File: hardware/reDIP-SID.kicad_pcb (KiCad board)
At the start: 4 copper layers, 17.8 x 35.6 mm, 90 parts, among them J1 Conn_01x04, J2 Conn_01x04, J3 Conn_01x10, J4 Conn_01x10, J5 TYPE-C-31-M-12, J6 Conn_02x05_Odd_Even, SW1 KXT331LHS, U1 NCP115AMX120TCG, U2 NCP167AMX330TBG, U3 SN74CBTD16211DGVR, U4 SGTL5000XNLA3, U5 NUF2042XV6, U6 APS6404L-3SQR-SN, U7 W25Q128JVPIM, U8 ICE40UP5K-SG48I, X1 ECS-1612MV-240-CN-TR

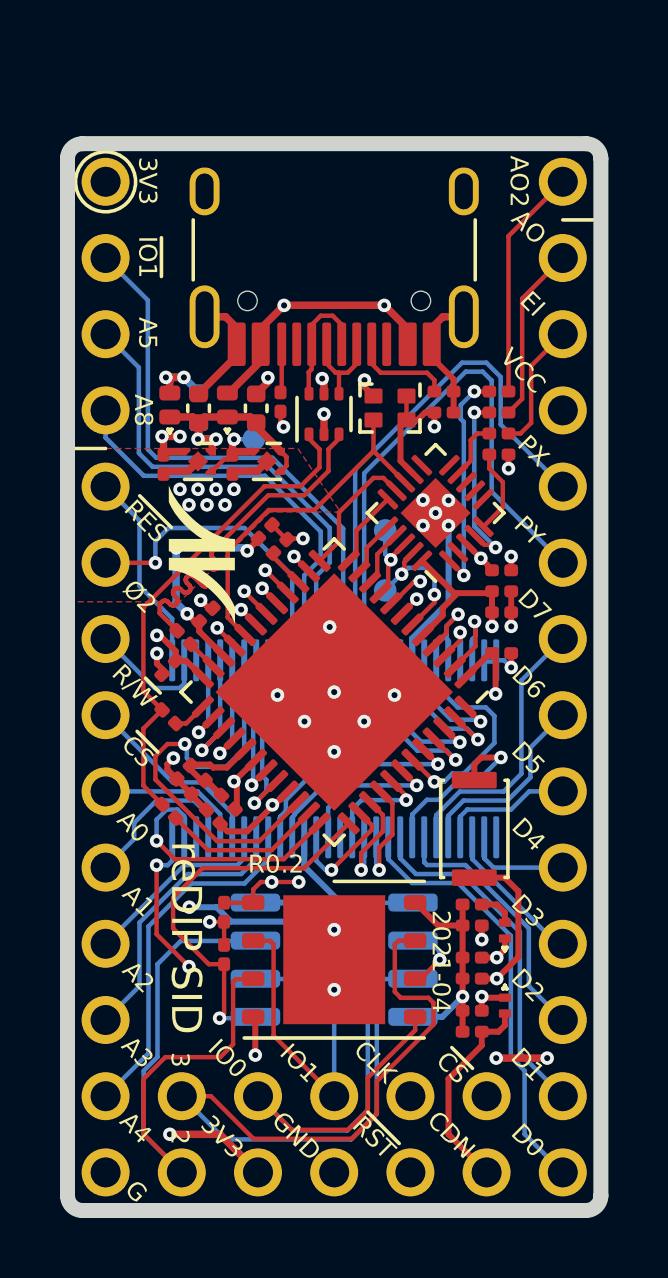
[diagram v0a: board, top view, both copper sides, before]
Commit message: Revision 1.0
The board has been revised to remedy a few shortcomings on the first prototype:

* Added a separate LDO for the SGTL5000 VDDD, to keep the iCE40 VCC at 1.2V.
* Added DC bias for AUDIO_OUT, required by the C64 audio output stage.
* Increased board length by 2.54mm, facilitating some notable enhancements:
  - Symmetric stereo input (EXT_IN and EXT_IN_R). Note: External AC coupling.
  - Symmetric stereo output (AOUT_L and AOUT_R) in addition to AUDIO_OUT.
  - USB receptacle flush with board edge.
  - Fully 6581 / 8580 pin compatible.

Big thanks go to @smunaut, who has not only implemented support for the
reDIP SID in his [no2bootloader](https://github.com/no2fpga/no2bootloader),
but has also provided invaluable feedback from his testing of prototypes.
He pointed out that the internal SGTL5000 voltage regulator forced the
1.2V rail up to unsafe levels for the iCE40, and that DC bias is required
to drive the C64 audio output stage. He also suggested to add symmetric
stereo output, in addition to the SID audio output.
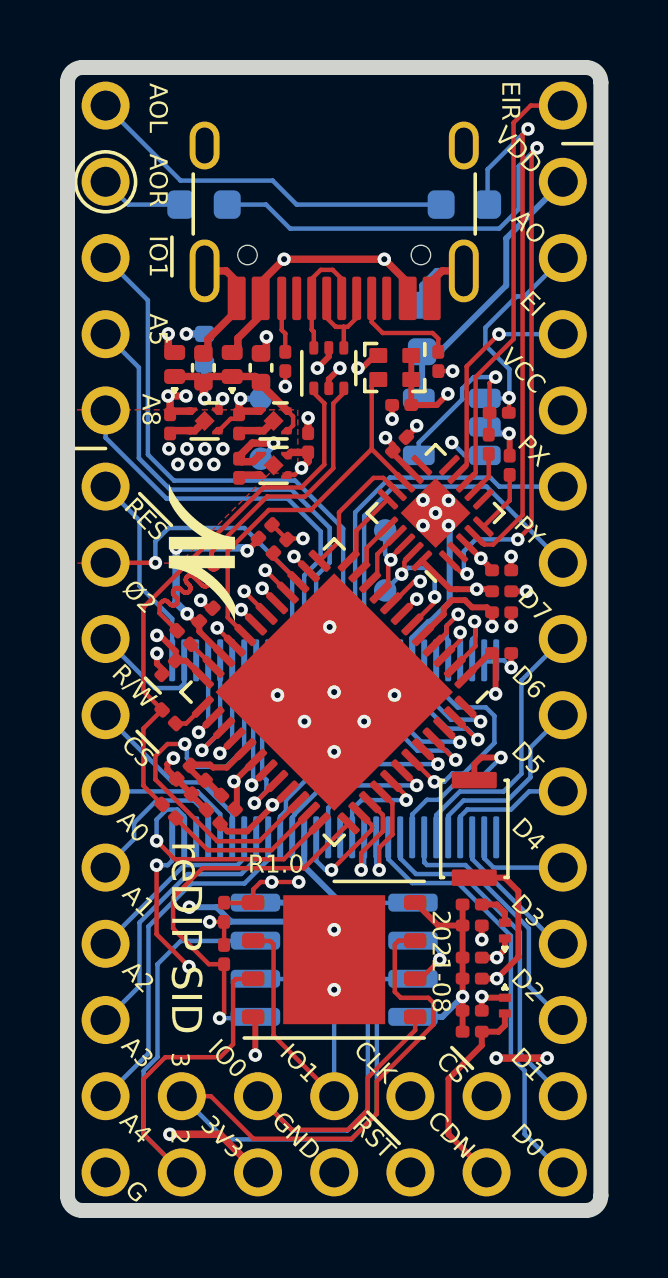
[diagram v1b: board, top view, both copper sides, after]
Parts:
- removed the C10 at (113.1, 107.7)
- removed the C15 at (113.2, 114.3)
- removed the C8 at (113.1, 108.4)
- removed the C9 at (113.1, 107.0)
- removed the J4 at (115.2, 110.2)
- removed the R4 at (105.8, 107.3)
- removed the SolderMask D0.5mm at (103.4, 110.8) (x2)
- removed the SolderMask D0.5mm at (102.8, 110.8) (x2)
- removed the SolderMask D0.5mm at (102.5, 110.2)
- removed the SolderMask D0.5mm at (103.1, 110.2) (x2)
- removed the SolderMask D0.5mm at (103.7, 110.2) (x2)
- removed the SolderMask D0.5mm at (104.0, 110.8) (x2)
- removed the SolderMask D0.5mm at (105.7, 117.1)
- removed the SolderMask D0.5mm at (107.6, 119.0)
- removed the SolderMask D0.5mm at (108.6, 118.0)
- removed the SolderMask D0.5mm at (109.6, 117.1)
- removed the SolderMask D0.5mm at (107.5, 114.8)
- removed the SolderMask D0.5mm at (107.6, 117.0)
- removed the SolderMask D0.5mm at (106.6, 118.0)
- removed the SolderMask D0.5mm at (104.3, 110.2)
- added C11: 1uF, Capacitor_SMD:C_0603_1608Metric, B.Cu at (110.5, 104.9)
- added C12: 10uF, Capacitor_SMD:C_0603_1608Metric, B.Cu at (103.3, 100.8)
- added C13: 10uF, Capacitor_SMD:C_0603_1608Metric, B.Cu at (112.0, 100.8)
- added C23: 0.1uF, Capacitor_SMD:C_0201_0603Metric, F.Cu at (109.9, 107.4)
- added C5: 1uF, Capacitor_SMD:C_0201_0603Metric, F.Cu at (106.8, 108.7)
- added C6: 1uF, Capacitor_SMD:C_0201_0603Metric, F.Cu at (104.5, 109.5)
- added C7: 0.1uF, Capacitor_SMD:C_0201_0603Metric, F.Cu at (113.2, 113.7)
- added J3: Conn_01x14, reDIP:PinHeader_1x14_P2.54mm_Vertical, B.Cu at (115.2, 100.0)
- added R3: 10k, Resistor_SMD:R_0201_0603Metric, F.Cu at (112.8, 108.8)
- added R5: 10k, Resistor_SMD:R_0201_0603Metric, F.Cu at (113.1, 107.7)
- added R6: 5.1k, Resistor_SMD:R_0201_0603Metric, F.Cu at (106.0, 106.0)
- added SolderMask D0.5mm: SolderMask_D0.5mm, reDIP:SolderMask_D0.5mm, B.Cu at (103.0, 109.4)
- added SolderMask D0.5mm: SolderMask_D0.5mm, reDIP:SolderMask_D0.5mm, B.Cu at (102.4, 109.4)
- added SolderMask D0.5mm: SolderMask_D0.5mm, reDIP:SolderMask_D0.5mm, B.Cu at (102.1, 108.9)
- added SolderMask D0.5mm: SolderMask_D0.5mm, reDIP:SolderMask_D0.5mm, B.Cu at (102.7, 108.9)
- added SolderMask D0.5mm: SolderMask_D0.5mm, reDIP:SolderMask_D0.5mm, B.Cu at (103.3, 108.9)
- added SolderMask D0.5mm: SolderMask_D0.5mm, reDIP:SolderMask_D0.5mm, B.Cu at (103.6, 109.4)
- added SolderMask D0.5mm: SolderMask_D0.3mm, reDIP:SolderMask_D0.3mm, F.Cu at (103.6, 109.4)
- added SolderMask D0.5mm: SolderMask_D0.3mm, reDIP:SolderMask_D0.3mm, F.Cu at (103.0, 109.4)
- added SolderMask D0.5mm: SolderMask_D0.3mm, reDIP:SolderMask_D0.3mm, F.Cu at (102.4, 109.4)
- added SolderMask D0.5mm: SolderMask_D0.3mm, reDIP:SolderMask_D0.3mm, F.Cu at (103.9, 108.9)
- added SolderMask D0.5mm: SolderMask_D0.3mm, reDIP:SolderMask_D0.3mm, F.Cu at (103.3, 108.9)
- added SolderMask D0.5mm: SolderMask_D0.3mm, reDIP:SolderMask_D0.3mm, F.Cu at (102.7, 108.9)
- added SolderMask_D0.3mm: SolderMask_D0.3mm, reDIP:SolderMask_D0.3mm, B.Cu at (107.6, 119.0)
- added SolderMask_D0.3mm: SolderMask_D0.3mm, reDIP:SolderMask_D0.3mm, B.Cu at (108.6, 118.0)
- added SolderMask_D0.3mm: SolderMask_D0.3mm, reDIP:SolderMask_D0.3mm, B.Cu at (106.6, 118.0)
- added SolderMask_D0.3mm: SolderMask_D0.3mm, reDIP:SolderMask_D0.3mm, B.Cu at (109.6, 117.1)
- added SolderMask_D0.3mm: SolderMask_D0.3mm, reDIP:SolderMask_D0.3mm, B.Cu at (107.6, 117.0)
- added SolderMask_D0.3mm: SolderMask_D0.3mm, reDIP:SolderMask_D0.3mm, B.Cu at (105.7, 117.1)
- added SolderMask_D0.3mm: SolderMask_D0.3mm, reDIP:SolderMask_D0.3mm, B.Cu at (107.5, 114.8)
- added TP2: TestPoint_Flag, reDIP:TestPoint_Pad_D0.75mm, B.Cu at (105.2, 109.2)
- added U3: NCP115AMX120TCG, ONSemi:CASE_711AJ_1.0x1.0mm_P0.65mm, F.Cu at (105.6, 109.5)
- added U7: MCP6H01T-E/OT, reDIP:SOT-23-5, B.Cu at (111.5, 108.2)
- added svg2mod: G***, reDIP:Nimrod-N, B.Cu at (108.4, 108.5)
- J1: value Conn_01x04 -> Conn_01x01; footprint reDIP:PinHeader_1x04_P2.54mm_Vertical_LongTail -> reDIP:PinHeader_1x01_P2.54mm_Vertical; moved to F.Cu
- J2: value Conn_01x04 -> Conn_01x05; footprint reDIP:PinHeader_1x04_P2.54mm_Vertical_LongTail -> reDIP:PinHeader_1x05_P2.54mm_Vertical; moved to F.Cu
- U8: renamed from U6; value APS6404L-3SQR-SN -> LY68L6400SLIT
- X1: value ECS-1612MV-240-CN-TR -> ASCO-24.000MHZ-EK-T3
- svg2mod: footprint reDIP:Nimrod-logo -> reDIP:Nimrod-text
- moved J1 15.5 mm to (115.2, 97.5), turned to 0 degrees
- moved J2 15.5 mm to (100.0, 97.5), turned to 0 degrees
- moved svg2mod 2.78 mm to (112.3, 112.5)
- moved JP1 1.96 mm to (103.3, 105.6)
- moved C8 1.81 mm to (109.8, 108.7), turned to 45 degrees
- moved MOS logo 1.55 mm to (106.0, 103.3)
- moved U6 1.54 mm to (107.4, 106.2)
- moved J5 1.53 mm to (107.6, 99.8)
- moved SolderMask D0.5mm 1.40 mm to (103.9, 108.9)
- moved SolderMask D0.5mm 1.40 mm to (102.1, 108.9)
- moved TP1 1.37 mm to (105.2, 107.2)
- moved C2 1.37 mm to (104.5, 108.1)
- moved C4 1.37 mm to (102.2, 108.1)
- moved U1 1.37 mm to (105.6, 108.0)
- moved U2 1.37 mm to (103.3, 108.0)
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- renumbered C7 to C10, C11 to C14, C12 to C15, C13 to C16, C14 to C17, C16 to C18, C17 to C19, C18 to C20, C19 to C21, C20 to C22, C5 to C8, C6 to C9, J3 to J4, R8 to R10, R9 to R11, R10 to R12, R11 to R13, R12 to R14, R13 to R15, R14 to R16, R3 to R4, R5 to R7, R6 to R8, R7 to R9, TP2 to TP3, TP3 to TP4, U8 to U10, U3 to U4, U4 to U5, U5 to U6, U7 to U9
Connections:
- J1 pad 1: +3V3 -> /EXT_IN_R
- J2 pad 1: /AUDIO_OUT_2 -> /AOUT_L
- J2 pad 2: /AUDIO_OUT -> /AOUT_R
- J2 pad 3: /EXT_IN -> /~IO1~
- J2 pad 4: VCC -> /A5
- U5 pad 20: +1V2 -> VDDD
- U5 pad 7: (no net) -> Net-(R3-Pad2)
- U5 pad 8: (no net) -> /EXT_IN_R
- U5 pad 9: Net-(C8-Pad1) -> /EXT_IN
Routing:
- net Net-(C12-Pad1): track 7.55 -> 29.5 mm, vias 2 -> 3
- net VDDD: track 0.00 -> 15.0 mm, vias 0 -> 2
- net /EXT_IN_R: track 0.00 -> 14.5 mm
- net /AOUT_L: track 0.00 -> 12.6 mm
- net Net-(C13-Pad1): track 6.15 -> 18.1 mm, vias 2 -> 1
- net VDD: track 0.00 -> 9.52 mm
- net /AUDIO_OUT_2: track 7.75 -> 0.00 mm
- net /POT_Y: track 19.1 -> 12.9 mm
- net Net-(R3-Pad1): track 0.00 -> 6.11 mm, vias 0 -> 1
- net /POT_X: track 17.4 -> 12.5 mm
- net GND: track 44.9 -> 48.8 mm, vias 36 -> 41
- net +3V3: track 37.8 -> 41.2 mm, vias 15 -> 18
- net /EXT_IN: track 4.29 -> 7.35 mm, vias 0 -> 1
- net /AOUT_R: track 0.00 -> 2.82 mm
- net Net-(C8-Pad1): track 2.03 -> 0.00 mm
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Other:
- board size 17.8 x 35.6 mm -> 17.8 x 38.1 mm
- board text added: "2021-08"
- board text added: "38.10 mm"
- board text added: "AOL"
- board text added: "AOR"
- board text added: "EIR"
- board text added: "R1.0"
- board text added: "VDD"
- board text added: "VDDD"
- board text removed: "1"
- board text removed: "2021-04"
- board text removed: "28"
- board text removed: "35.56 mm"
- board text removed: "AO2"
- board text removed: "No SID pins!"
- board text removed: "R0.2"

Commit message: Hardware mixing of left and right channels to AUDIO_OUT
As suggested by @smunaut.
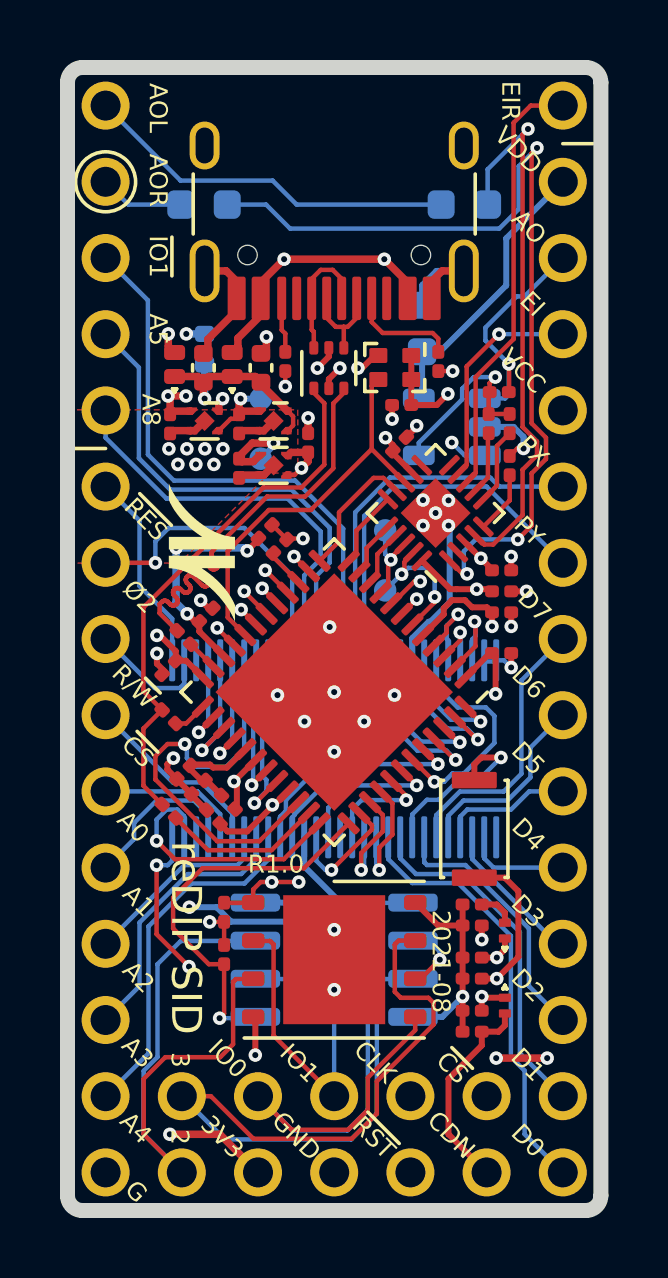
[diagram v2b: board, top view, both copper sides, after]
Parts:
- removed the R3 at (112.8, 108.8)
- added R4: 20k, Resistor_SMD:R_0201_0603Metric, F.Cu at (112.8, 108.1)
- added R6: 10k, Resistor_SMD:R_0201_0603Metric, F.Cu at (113.1, 107.0)
- R5: value 10k -> 20k
- moved R5 0.50 mm to (113.5, 108.1), turned to 270 degrees
- renumbered R9 to R10, R10 to R11, R11 to R12, R12 to R13, R13 to R14, R14 to R15, R15 to R16, R16 to R17, R4 to R3, R6 to R7, R7 to R8, R8 to R9
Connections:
- R5 pad 1: /AUDIO_OUT -> Net-(R4-Pad1)
- R5 pad 2: Net-(R3-Pad1) -> Net-(R5-Pad2)
- U5 pad 6: (no net) -> Net-(R5-Pad2)
- U7 pad 4: Net-(R3-Pad1) -> Net-(R4-Pad1)
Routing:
- net Net-(R3-Pad1): track 6.11 -> 0.00 mm, vias 1 -> 0
- net Net-(R4-Pad1): track 0.00 -> 6.11 mm, vias 0 -> 1
- net Net-(R5-Pad2): track 0.00 -> 2.56 mm
- net GND: track 48.8 -> 50.1 mm
- net Net-(R4-Pad2): track 1.42 -> 2.11 mm

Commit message: Changed to machined (round) pin headers
This allows the board to be mounted directly in a SID socket.

Thanks to @smunaut for the pin header 3D models.
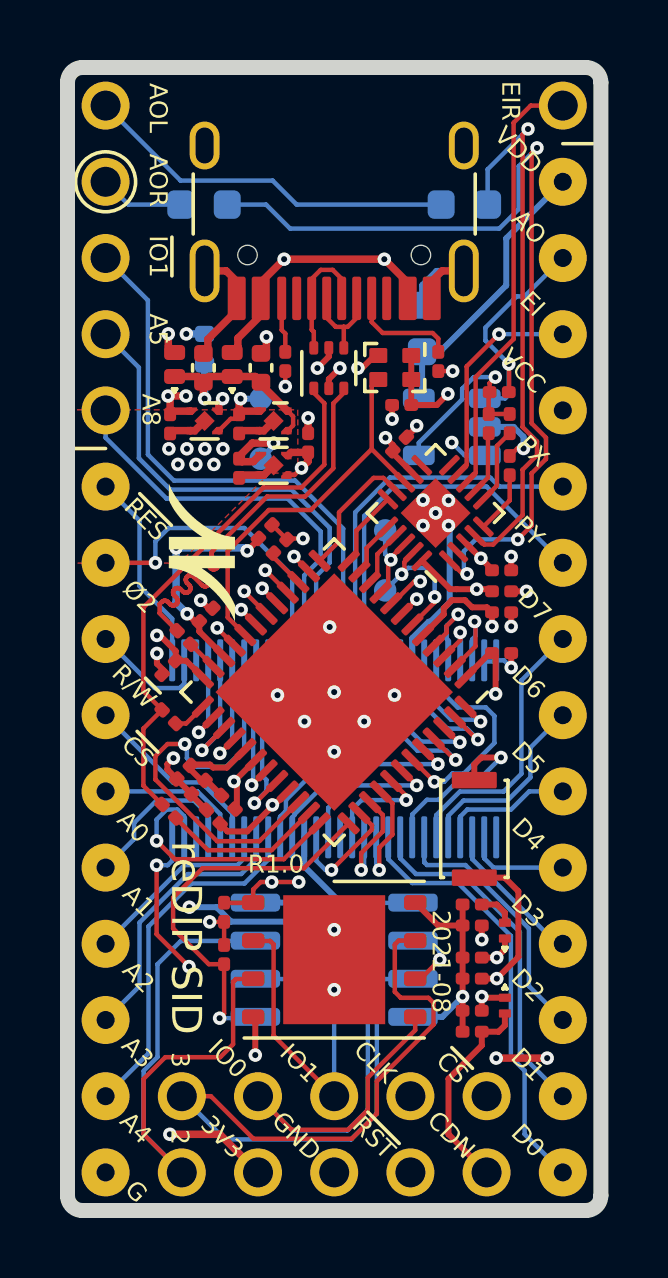
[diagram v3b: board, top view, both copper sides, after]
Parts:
- removed SolderMask D0.5mm: SolderMask_D0.5mm, reDIP:SolderMask_D0.5mm (x6)
- removed SolderMask D0.5mm: SolderMask_D0.3mm, reDIP:SolderMask_D0.3mm (x6)
- added SolderMask_D0.3mm: SolderMask_D0.3mm, reDIP:SolderMask_D0.3mm, F.Cu at (102.4, 109.4)
- added SolderMask_D0.3mm: SolderMask_D0.3mm, reDIP:SolderMask_D0.3mm, F.Cu at (103.9, 108.9)
- added SolderMask_D0.3mm: SolderMask_D0.3mm, reDIP:SolderMask_D0.3mm, F.Cu at (103.3, 108.9)
- added SolderMask_D0.3mm: SolderMask_D0.3mm, reDIP:SolderMask_D0.3mm, F.Cu at (102.7, 108.9)
- added SolderMask_D0.3mm: SolderMask_D0.3mm, reDIP:SolderMask_D0.3mm, F.Cu at (103.6, 109.4)
- added SolderMask_D0.3mm: SolderMask_D0.3mm, reDIP:SolderMask_D0.3mm, F.Cu at (103.0, 109.4)
- added SolderMask_D0.5mm: SolderMask_D0.5mm, reDIP:SolderMask_D0.5mm, B.Cu at (103.0, 109.4)
- added SolderMask_D0.5mm: SolderMask_D0.5mm, reDIP:SolderMask_D0.5mm, B.Cu at (102.4, 109.4)
- added SolderMask_D0.5mm: SolderMask_D0.5mm, reDIP:SolderMask_D0.5mm, B.Cu at (102.1, 108.9)
- added SolderMask_D0.5mm: SolderMask_D0.5mm, reDIP:SolderMask_D0.5mm, B.Cu at (102.7, 108.9)
- added SolderMask_D0.5mm: SolderMask_D0.5mm, reDIP:SolderMask_D0.5mm, B.Cu at (103.3, 108.9)
- added SolderMask_D0.5mm: SolderMask_D0.5mm, reDIP:SolderMask_D0.5mm, B.Cu at (103.6, 109.4)
- J3: footprint reDIP:PinHeader_1x14_P2.54mm_Vertical -> reDIP:PinHeader_1x14_P2.54mm_Vertical_Machined
- J4: footprint reDIP:PinHeader_1x10_P2.54mm_Vertical -> reDIP:PinHeader_1x10_P2.54mm_Vertical_Machined
- SolderMask_D0.3mm, SolderMask_D0.5mm (x8): renamed from SolderMask D0.5mm
- moved svg2mod 0.30 mm to (108.7, 108.5)
